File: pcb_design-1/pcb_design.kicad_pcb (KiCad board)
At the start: 2 copper layers, 24 x 61.5 mm, 4 parts, among them SW1 SW_Push, SW2 SW_Push, SW3 SW_Push, U1 MOUDLE-SEEEDUINO-XIAO

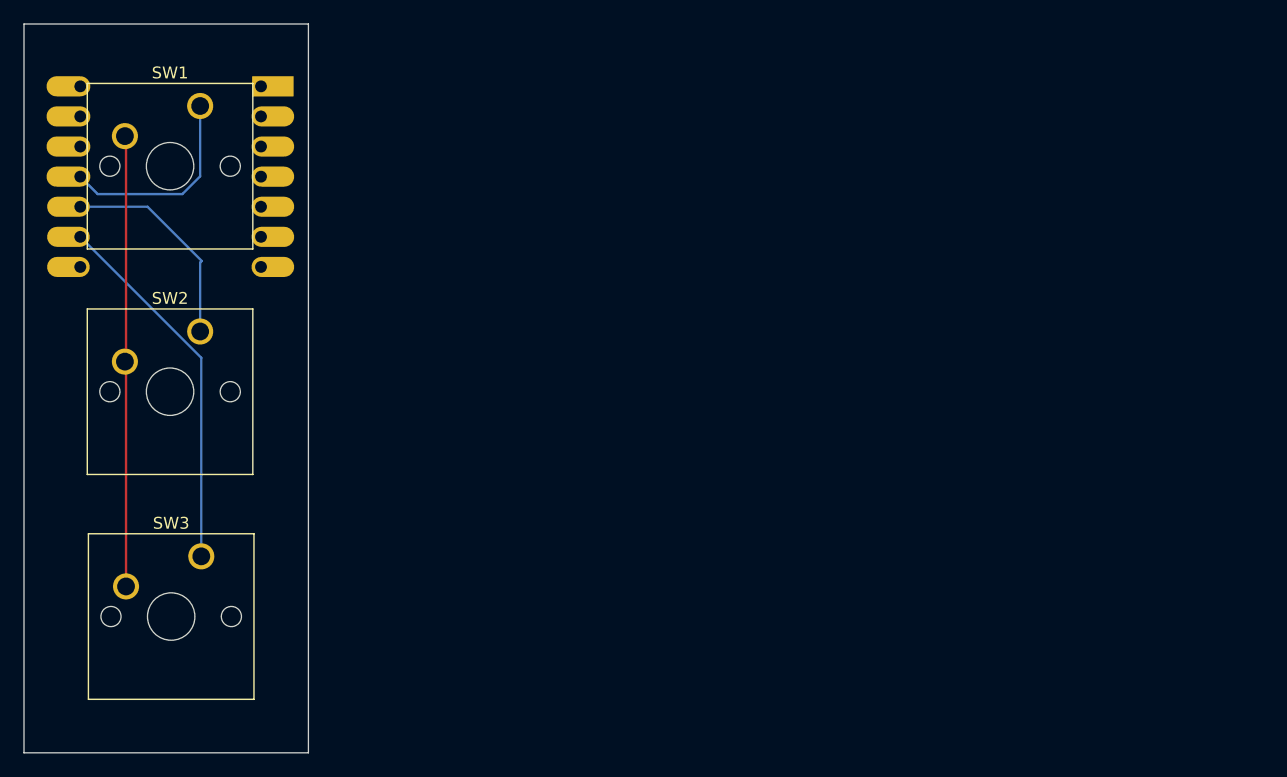
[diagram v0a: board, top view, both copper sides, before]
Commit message: Polish codebase: complete macro pad firmware, update KiCad project files, and add detailed README documentation with schematic/PCB renders
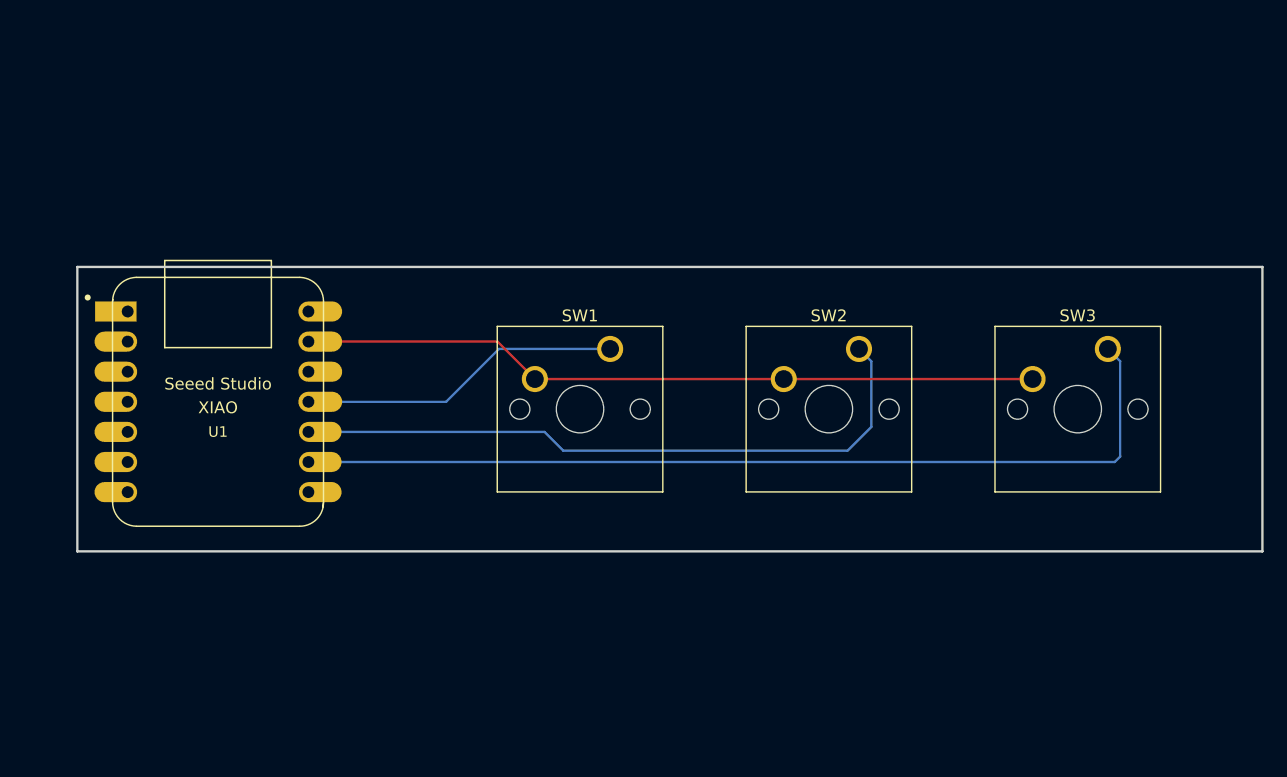
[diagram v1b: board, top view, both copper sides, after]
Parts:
- U1: moved to F.Cu
- moved SW3 78.5 mm to (194.0, 88.9)
- moved SW2 55.6 mm to (173.0, 88.9)
- moved SW1 40.2 mm to (152.0, 88.9)
- moved U1 19.4 mm to (118.9, 93.4), turned to 0 degrees
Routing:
- net Net-(U1-PA7_A8_D8_SCK): track 31.2 -> 78.2 mm
- net Net-(U1-PA5_A9_D9_MISO): track 18.2 -> 56.0 mm
- net GND: track 38.0 -> 62.4 mm
- net Net-(U1-PA6_A10_D10_MOSI): track 17.3 -> 27.3 mm
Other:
- board size 24 x 61.5 mm -> 100 x 24 mm
